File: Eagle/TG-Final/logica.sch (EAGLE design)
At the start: 1 part, among them U1 ARDUINO_SHIELDLONGPADS

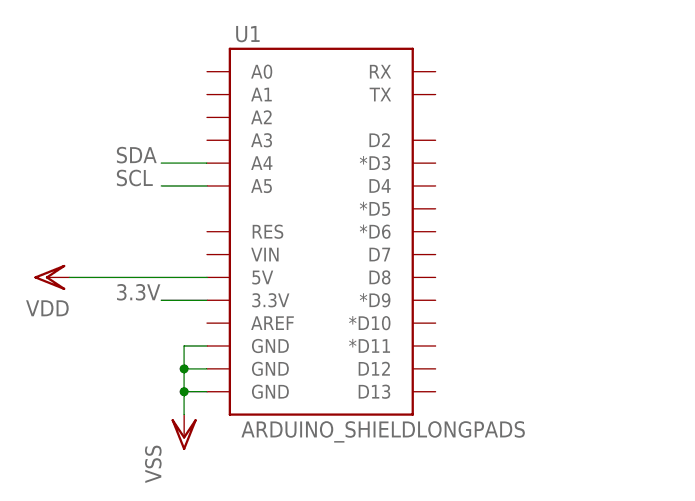
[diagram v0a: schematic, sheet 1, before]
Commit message: Esquematicos para placa logica
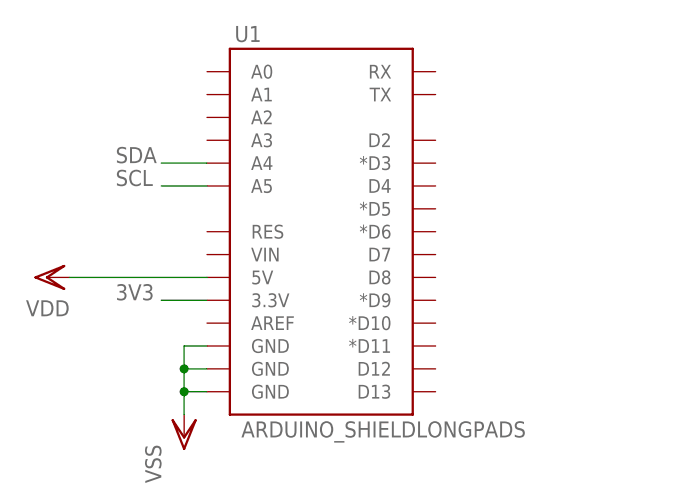
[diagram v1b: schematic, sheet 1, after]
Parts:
- added U$1: LOGIC-LEVEL-CONVERTER, aasanchez:LOGIC-LEVEL-CONVERTER
- added U$2: IMU3000COMBO, aasanchez:IMU3000COMBO
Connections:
- removed net 3.3V: U1.3.3V
- new net 3V3: U$1.LV, U$2.3V3, U1.3.3V
- new net N$1: U$1.TXI-1, U$2.SCL
- new net N$2: U$1.TXI-2, U$2.SDA
- net SCL: now also U$1.TXO-1
- net SDA: now also U$1.TXO-2
- net VDD: now also U$1.HV
- net VSS: now also U$1.GND, U$2.VSS
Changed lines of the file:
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@@
 <part name="VSS1" library="supply1" deviceset="VSS" device=""/>
 <part name="VDD1" library="supply1" deviceset="VDD" device=""/>
+<part name="U$2" library="aasanchez" deviceset="IMU3000COMBO" device=""/>
+<part name="VSS2" library="supply1" deviceset="VSS" device=""/>
+<part name="VSS3" library="supply1" deviceset="VSS" device=""/>
+<part name="VDD2" library="supply1" deviceset="VDD" device=""/>
+<part name="U$1" library="aasanchez" deviceset="LOGIC-LEVEL-CONVERTER" device=""/>
 </parts>
 <sheets>
@@
 </segment>
 </net>
-<net name="3.3V" class="0">
+<net name="3V3" class="0">
 <segment>
 <pinref part="U1" gate="G$1" pin="3.3V"/>
@@
 </plain>
 <instances>
+<instance part="U$2" gate="G$1" x="68.58" y="50.8"/>
+<instance part="VSS2" gate="G$1" x="60.96" y="45.72"/>
+<instance part="VSS3" gate="G$1" x="45.72" y="63.5" rot="R90"/>
+<instance part="VDD2" gate="G$1" x="-5.08" y="60.96" rot="R90"/>
+<instance part="U$1" gate="G$1" x="30.48" y="76.2" rot="R180"/>
 </instances>
 <busses>
 </busses>
 <nets>
+<net name="3V3" class="0">
+<segment>
+<wire x1="43.18" y1="60.96" x2="43.18" y2="53.34" width="0.1524" layer="91"/>
+<pinref part="U$2" gate="G$1" pin="3V3"/>
+<wire x1="43.18" y1="53.34" x2="63.5" y2="53.34" width="0.1524" layer="91"/>
+<pinref part="U$1" gate="G$1" pin="LV"/>
+<wire x1="43.18" y1="60.96" x2="35.56" y2="60.96" width="0.1524" layer="91"/>
+</segment>
+</net>
+<net name="VSS" class="0">
+<segment>
+<pinref part="U$2" gate="G$1" pin="VSS"/>
+<wire x1="63.5" y1="55.88" x2="60.96" y2="55.88" width="0.1524" layer="91"/>
+<wire x1="60.96" y1="55.88" x2="60.96" y2="48.26" width="0.1524" layer="91"/>
+<pinref part="VSS2" gate="G$1" pin="VSS"/>
+</segment>
+<segment>
+<pinref part="VSS3" gate="G$1" pin="VSS"/>
+<pinref part="U$1" gate="G$1" pin="GND"/>
+<wire x1="43.18" y1="63.5" x2="35.56" y2="63.5" width="0.1524" layer="91"/>
+</segment>
+</net>
+<net name="VDD" class="0">
+<segment>
+<pinref part="U$1" gate="G$1" pin="HV"/>
+<pinref part="VDD2" gate="G$1" pin="VDD"/>
+<wire x1="5.08" y1="60.96" x2="-2.54" y2="60.96" width="0.1524" layer="91"/>
+</segment>
+</net>
+<net name="SCL" class="0">
+<segment>
+<pinref part="U$1" gate="G$1" pin="TXO-1"/>
+<wire x1="5.08" y1="53.34" x2="0" y2="53.34" width="0.1524" layer="91"/>
+<label x="-5.08" y="53.34" size="1.778" layer="95"/>
+</segment>
+</net>
+<net name="SDA" class="0">
+<segment>
+<pinref part="U$1" gate="G$1" pin="TXO-2"/>
+<wire x1="5.08" y1="71.12" x2="0" y2="71.12" width="0.1524" layer="91"/>
+<label x="-5.08" y="71.12" size="1.778" layer="95"/>
+</segment>
+</net>
+<net name="N$1" class="0">
+<segment>
+<pinref part="U$1" gate="G$1" pin="TXI-1"/>
+<wire x1="35.56" y1="53.34" x2="40.64" y2="53.34" width="0.1524" layer="91"/>
+<wire x1="40.64" y1="53.34" x2="40.64" y2="50.8" width="0.1524" layer="91"/>
+<wire x1="40.64" y1="50.8" x2="58.42" y2="50.8" width="0.1524" layer="91"/>
+<wire x1="58.42" y1="50.8" x2="58.42" y2="60.96" width="0.1524" layer="91"/>
+<pinref part="U$2" gate="G$1" pin="SCL"/>
+<wire x1="58.42" y1="60.96" x2="63.5" y2="60.96" width="0.1524" layer="91"/>
+</segment>
+</net>
+<net name="N$2" class="0">
+<segment>
+<pinref part="U$1" gate="G$1" pin="TXI-2"/>
+<wire x1="35.56" y1="71.12" x2="53.34" y2="71.12" width="0.1524" layer="91"/>
+<wire x1="53.34" y1="71.12" x2="53.34" y2="58.42" width="0.1524" layer="91"/>
+<pinref part="U$2" gate="G$1" pin="SDA"/>
+<wire x1="53.34" y1="58.42" x2="63.5" y2="58.42" width="0.1524" layer="91"/>
+</segment>
+</net>
 </nets>
 </sheet>

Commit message: Fix Pins Motor 1, Avances en Esquematicos
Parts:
- added U$3: UK1122, aasanchez:UK1122
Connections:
- new net +12V: U$3.+
- new net D13: U$3.IN1, U1.D13
- new net N$13: U$3.ENA
- new net N$14: U$3.IN2
- new net N$15: U$3.IN3
- new net N$16: U$3.ENB
- new net N$17: U$3.IN4
- new net N$4: U1.D12
- new net N$5: U1.*D11
- new net N$6: U1.*D9
- new net N$8: U1.D8
- new net N$9: U1.D7
- new net SERVO-01: U1.*D10
- net 3V3: now also U$2.VCC; no longer U$2.3V3
- net VDD: now also U$3.+5
- net VSS: now also U$2.GND, U$3.-, U$3.CSA, U$3.CSB, U$3.GND; no longer U$2.VSS
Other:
- note added: "ENA"
- note added: "IN1"
- note added: "IN2"
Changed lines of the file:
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@@
 <part name="VDD2" library="supply1" deviceset="VDD" device=""/>
 <part name="U$1" library="aasanchez" deviceset="LOGIC-LEVEL-CONVERTER" device=""/>
+<part name="U$3" library="aasanchez" deviceset="UK1122" device=""/>
+<part name="VSS4" library="supply1" deviceset="VSS" device=""/>
+<part name="P+1" library="supply1" deviceset="+12V" device=""/>
+<part name="VDD3" library="supply1" deviceset="VDD" device=""/>
 </parts>
 <sheets>
@@
 <description>Arduino</description>
 <plain>
+<text x="91.44" y="45.72" size="1.778" layer="95">IN1</text>
+<text x="91.44" y="48.26" size="1.778" layer="95">IN2</text>
+<text x="91.44" y="50.8" size="1.778" layer="95">ENA</text>
 </plain>
 <instances>
@@
 <wire x1="63.5" y1="71.12" x2="58.42" y2="71.12" width="0.1524" layer="91"/>
 <label x="53.34" y="71.12" size="1.778" layer="95"/>
+</segment>
+</net>
+<net name="D13" class="0">
+<segment>
+<pinref part="U1" gate="G$1" pin="D13"/>
+<wire x1="88.9" y1="45.72" x2="91.44" y2="45.72" width="0.1524" layer="91"/>
+</segment>
+</net>
+<net name="N$4" class="0">
+<segment>
+<pinref part="U1" gate="G$1" pin="D12"/>
+<wire x1="88.9" y1="48.26" x2="91.44" y2="48.26" width="0.1524" layer="91"/>
+</segment>
+</net>
+<net name="N$5" class="0">
+<segment>
+<pinref part="U1" gate="G$1" pin="*D11"/>
+<wire x1="88.9" y1="50.8" x2="91.44" y2="50.8" width="0.1524" layer="91"/>
+</segment>
+</net>
+<net name="N$6" class="0">
+<segment>
+<pinref part="U1" gate="G$1" pin="*D9"/>
+<wire x1="88.9" y1="55.88" x2="91.44" y2="55.88" width="0.1524" layer="91"/>
+</segment>
+</net>
+<net name="SERVO-01" class="0">
+<segment>
+<pinref part="U1" gate="G$1" pin="*D10"/>
+<wire x1="88.9" y1="53.34" x2="96.52" y2="53.34" width="0.1524" layer="91"/>
+<label x="96.52" y="53.34" size="1.778" layer="95"/>
+</segment>
+</net>
+<net name="N$8" class="0">
+<segment>
+<pinref part="U1" gate="G$1" pin="D8"/>
+<wire x1="88.9" y1="58.42" x2="91.44" y2="58.42" width="0.1524" layer="91"/>
+</segment>
+</net>
+<net name="N$9" class="0">
+<segment>
+<pinref part="U1" gate="G$1" pin="D7"/>
+<wire x1="88.9" y1="60.96" x2="91.44" y2="60.96" width="0.1524" layer="91"/>
 </segment>
 </net>
@@
 <segment>
 <wire x1="43.18" y1="60.96" x2="43.18" y2="53.34" width="0.1524" layer="91"/>
-<pinref part="U$2" gate="G$1" pin="3V3"/>
+<pinref part="U$2" gate="G$1" pin="VCC"/>
 <wire x1="43.18" y1="53.34" x2="63.5" y2="53.34" width="0.1524" layer="91"/>
 <pinref part="U$1" gate="G$1" pin="LV"/>
@@
 <net name="VSS" class="0">
 <segment>
-<pinref part="U$2" gate="G$1" pin="VSS"/>
+<pinref part="U$2" gate="G$1" pin="GND"/>
 <wire x1="63.5" y1="55.88" x2="60.96" y2="55.88" width="0.1524" layer="91"/>
 <wire x1="60.96" y1="55.88" x2="60.96" y2="48.26" width="0.1524" layer="91"/>
@@
 </plain>
 <instances>
+<instance part="U$3" gate="G$1" x="0" y="0"/>
+<instance part="VSS4" gate="G$1" x="12.7" y="-10.16"/>
+<instance part="P+1" gate="1" x="0" y="-2.54" rot="R90"/>
+<instance part="VDD3" gate="G$1" x="20.32" y="-17.78" rot="R180"/>
 </instances>
 <busses>
 </busses>
 <nets>
+<net name="VSS" class="0">
+<segment>
+<pinref part="U$3" gate="G$1" pin="-"/>
+<wire x1="7.62" y1="0" x2="7.62" y2="-2.54" width="0.1524" layer="91"/>
+<wire x1="7.62" y1="-2.54" x2="12.7" y2="-2.54" width="0.1524" layer="91"/>
+<pinref part="U$3" gate="G$1" pin="GND"/>
+<wire x1="12.7" y1="-2.54" x2="17.78" y2="-2.54" width="0.1524" layer="91"/>
+<wire x1="17.78" y1="-2.54" x2="17.78" y2="0" width="0.1524" layer="91"/>
+<wire x1="17.78" y1="-2.54" x2="30.48" y2="-2.54" width="0.1524" layer="91"/>
+<pinref part="U$3" gate="G$1" pin="CSA"/>
+<wire x1="30.48" y1="-2.54" x2="30.48" y2="0" width="0.1524" layer="91"/>
+<pinref part="U$3" gate="G$1" pin="CSB"/>
+<wire x1="40.64" y1="0" x2="40.64" y2="-2.54" width="0.1524" layer="91"/>
+<wire x1="40.64" y1="-2.54" x2="30.48" y2="-2.54" width="0.1524" layer="91"/>
+<pinref part="VSS4" gate="G$1" pin="VSS"/>
+<wire x1="12.7" y1="-7.62" x2="12.7" y2="-2.54" width="0.1524" layer="91"/>
+<junction x="12.7" y="-2.54"/>
+<junction x="17.78" y="-2.54"/>
+<junction x="30.48" y="-2.54"/>
+</segment>
+</net>
+<net name="+12V" class="0">
+<segment>
+<pinref part="P+1" gate="1" pin="+12V"/>
+<wire x1="2.54" y1="-2.54" x2="5.08" y2="-2.54" width="0.1524" layer="91"/>
+<pinref part="U$3" gate="G$1" pin="+"/>
+<wire x1="5.08" y1="-2.54" x2="5.08" y2="0" width="0.1524" layer="91"/>
+</segment>
+</net>
+<net name="VDD" class="0">
+<segment>
+<pinref part="VDD3" gate="G$1" pin="VDD"/>
+<pinref part="U$3" gate="G$1" pin="+5"/>
+<wire x1="20.32" y1="-15.24" x2="20.32" y2="0" width="0.1524" layer="91"/>
+</segment>
+</net>
+<net name="D13" class="0">
+<segment>
+<pinref part="U$3" gate="G$1" pin="IN1"/>
+<wire x1="22.86" y1="0" x2="22.86" y2="-7.62" width="0.1524" layer="91"/>
+<label x="22.86" y="-7.62" size="1.778" layer="95" rot="R270"/>
+</segment>
+</net>
+<net name="N$13" class="0">
+<segment>
+<pinref part="U$3" gate="G$1" pin="ENA"/>
+<wire x1="25.4" y1="0" x2="25.4" y2="-7.62" width="0.1524" layer="91"/>
+</segment>
+</net>
+<net name="N$14" class="0">
+<segment>
+<pinref part="U$3" gate="G$1" pin="IN2"/>
+<wire x1="27.94" y1="0" x2="27.94" y2="-7.62" width="0.1524" layer="91"/>
+</segment>
+</net>
+<net name="N$15" class="0">
+<segment>
+<pinref part="U$3" gate="G$1" pin="IN3"/>
+<wire x1="33.02" y1="0" x2="33.02" y2="-7.62" width="0.1524" layer="91"/>
+</segment>
+</net>
+<net name="N$16" class="0">
+<segment>
+<pinref part="U$3" gate="G$1" pin="ENB"/>
+<wire x1="35.56" y1="0" x2="35.56" y2="-7.62" width="0.1524" layer="91"/>
+</segment>
+</net>
+<net name="N$17" class="0">
+<segment>
+<pinref part="U$3" gate="G$1" pin="IN4"/>
+<wire x1="38.1" y1="0" x2="38.1" y2="-7.62" width="0.1524" layer="91"/>
+</segment>
+</net>
 </nets>
 </sheet>

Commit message: Placa de Actuadores y Otros
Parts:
- added U$4: BASE, aasanchez:BASE
- renumbered U$3 to L298
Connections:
- removed net N$13: L298.ENA
- removed net N$14: L298.IN2
- removed net N$15: L298.IN3
- removed net N$16: L298.ENB
- removed net N$17: L298.IN4
- removed net N$4: U1.D12
- removed net N$5: U1.*D11
- removed net N$6: U1.*D9
- removed net N$8: U1.D8
- removed net N$9: U1.D7
- new net D11: L298.ENA, U1.*D11
- new net D12: L298.IN2, U1.D12
- new net D7: L298.IN4, U1.D7
- new net D8: L298.IN3, U1.D8
- new net D9: L298.ENB, U1.*D9
- new net SERVO-02: U1.*D6
- new net SERVO-03: U1.*D5
- new net SERVO-04: U1.*D3
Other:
- note added: "ENB"
- note added: "IN3"
- note added: "IN4"
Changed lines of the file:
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@@
 <part name="VDD2" library="supply1" deviceset="VDD" device=""/>
 <part name="U$1" library="aasanchez" deviceset="LOGIC-LEVEL-CONVERTER" device=""/>
-<part name="U$3" library="aasanchez" deviceset="UK1122" device=""/>
+<part name="L298" library="aasanchez" deviceset="UK1122" device=""/>
 <part name="VSS4" library="supply1" deviceset="VSS" device=""/>
 <part name="P+1" library="supply1" deviceset="+12V" device=""/>
 <part name="VDD3" library="supply1" deviceset="VDD" device=""/>
+<part name="U$4" library="aasanchez" deviceset="BASE" device=""/>
 </parts>
 <sheets>
@@
 <text x="91.44" y="48.26" size="1.778" layer="95">IN2</text>
 <text x="91.44" y="50.8" size="1.778" layer="95">ENA</text>
+<text x="91.44" y="55.88" size="1.778" layer="95">ENB</text>
+<text x="91.44" y="58.42" size="1.778" layer="95">IN3</text>
+<text x="91.44" y="60.96" size="1.778" layer="95">IN4</text>
 </plain>
 <instances>
@@
 <instance part="VSS1" gate="G$1" x="60.96" y="40.64"/>
 <instance part="VDD1" gate="G$1" x="45.72" y="58.42" rot="R90"/>
+<instance part="U$4" gate="G$1" x="106.68" y="40.64"/>
 </instances>
 <busses>
@@
 </segment>
 </net>
-<net name="N$4" class="0">
+<net name="D12" class="0">
 <segment>
 <pinref part="U1" gate="G$1" pin="D12"/>
@@
 </segment>
 </net>
-<net name="N$5" class="0">
+<net name="D11" class="0">
 <segment>
 <pinref part="U1" gate="G$1" pin="*D11"/>
@@
 </segment>
 </net>
-<net name="N$6" class="0">
+<net name="D9" class="0">
 <segment>
 <pinref part="U1" gate="G$1" pin="*D9"/>
@@
 </segment>
 </net>
-<net name="N$8" class="0">
+<net name="D8" class="0">
 <segment>
 <pinref part="U1" gate="G$1" pin="D8"/>
@@
 </segment>
 </net>
-<net name="N$9" class="0">
+<net name="D7" class="0">
 <segment>
 <pinref part="U1" gate="G$1" pin="D7"/>
 <wire x1="88.9" y1="60.96" x2="91.44" y2="60.96" width="0.1524" layer="91"/>
+</segment>
+</net>
+<net name="SERVO-02" class="0">
+<segment>
+<pinref part="U1" gate="G$1" pin="*D6"/>
+<wire x1="88.9" y1="63.5" x2="96.52" y2="63.5" width="0.1524" layer="91"/>
+<label x="96.52" y="63.5" size="1.778" layer="95"/>
+</segment>
+</net>
+<net name="SERVO-03" class="0">
+<segment>
+<pinref part="U1" gate="G$1" pin="*D5"/>
+<wire x1="88.9" y1="66.04" x2="96.52" y2="66.04" width="0.1524" layer="91"/>
+<label x="96.52" y="66.04" size="1.778" layer="95"/>
+</segment>
+</net>
+<net name="SERVO-04" class="0">
+<segment>
+<pinref part="U1" gate="G$1" pin="*D3"/>
+<wire x1="88.9" y1="71.12" x2="96.52" y2="71.12" width="0.1524" layer="91"/>
+<label x="96.52" y="71.12" size="1.778" layer="95"/>
 </segment>
 </net>
@@
 </plain>
 <instances>
-<instance part="U$3" gate="G$1" x="0" y="0"/>
-<instance part="VSS4" gate="G$1" x="12.7" y="-10.16"/>
+<instance part="L298" gate="G$1" x="0" y="0"/>
+<instance part="VSS4" gate="G$1" x="12.7" y="-17.78"/>
 <instance part="P+1" gate="1" x="0" y="-2.54" rot="R90"/>
 <instance part="VDD3" gate="G$1" x="20.32" y="-17.78" rot="R180"/>
@@
 <net name="VSS" class="0">
 <segment>
-<pinref part="U$3" gate="G$1" pin="-"/>
+<pinref part="L298" gate="G$1" pin="-"/>
 <wire x1="7.62" y1="0" x2="7.62" y2="-2.54" width="0.1524" layer="91"/>
 <wire x1="7.62" y1="-2.54" x2="12.7" y2="-2.54" width="0.1524" layer="91"/>
-<pinref part="U$3" gate="G$1" pin="GND"/>
+<pinref part="L298" gate="G$1" pin="GND"/>
 <wire x1="12.7" y1="-2.54" x2="17.78" y2="-2.54" width="0.1524" layer="91"/>
 <wire x1="17.78" y1="-2.54" x2="17.78" y2="0" width="0.1524" layer="91"/>
 <wire x1="17.78" y1="-2.54" x2="30.48" y2="-2.54" width="0.1524" layer="91"/>
-<pinref part="U$3" gate="G$1" pin="CSA"/>
+<pinref part="L298" gate="G$1" pin="CSA"/>
 <wire x1="30.48" y1="-2.54" x2="30.48" y2="0" width="0.1524" layer="91"/>
-<pinref part="U$3" gate="G$1" pin="CSB"/>
+<pinref part="L298" gate="G$1" pin="CSB"/>
 <wire x1="40.64" y1="0" x2="40.64" y2="-2.54" width="0.1524" layer="91"/>
 <wire x1="40.64" y1="-2.54" x2="30.48" y2="-2.54" width="0.1524" layer="91"/>
 <pinref part="VSS4" gate="G$1" pin="VSS"/>
-<wire x1="12.7" y1="-7.62" x2="12.7" y2="-2.54" width="0.1524" layer="91"/>
+<wire x1="12.7" y1="-15.24" x2="12.7" y2="-2.54" width="0.1524" layer="91"/>
 <junction x="12.7" y="-2.54"/>
 <junction x="17.78" y="-2.54"/>
@@
 <pinref part="P+1" gate="1" pin="+12V"/>
 <wire x1="2.54" y1="-2.54" x2="5.08" y2="-2.54" width="0.1524" layer="91"/>
-<pinref part="U$3" gate="G$1" pin="+"/>
+<pinref part="L298" gate="G$1" pin="+"/>
 <wire x1="5.08" y1="-2.54" x2="5.08" y2="0" width="0.1524" layer="91"/>
 </segment>
@@
 <segment>
 <pinref part="VDD3" gate="G$1" pin="VDD"/>
-<pinref part="U$3" gate="G$1" pin="+5"/>
+<pinref part="L298" gate="G$1" pin="+5"/>
 <wire x1="20.32" y1="-15.24" x2="20.32" y2="0" width="0.1524" layer="91"/>
 </segment>
@@
 <net name="D13" class="0">
 <segment>
-<pinref part="U$3" gate="G$1" pin="IN1"/>
+<pinref part="L298" gate="G$1" pin="IN1"/>
 <wire x1="22.86" y1="0" x2="22.86" y2="-7.62" width="0.1524" layer="91"/>
 <label x="22.86" y="-7.62" size="1.778" layer="95" rot="R270"/>
 </segment>
 </net>
-<net name="N$13" class="0">
-<segment>
-<pinref part="U$3" gate="G$1" pin="ENA"/>
+<net name="D11" class="0">
+<segment>
+<pinref part="L298" gate="G$1" pin="ENA"/>
 <wire x1="25.4" y1="0" x2="25.4" y2="-7.62" width="0.1524" layer="91"/>
-</segment>
-</net>
-<net name="N$14" class="0">
-<segment>
-<pinref part="U$3" gate="G$1" pin="IN2"/>
+<label x="25.4" y="-7.62" size="1.778" layer="95" rot="R270"/>
+</segment>
+</net>
+<net name="D12" class="0">
+<segment>
+<pinref part="L298" gate="G$1" pin="IN2"/>
 <wire x1="27.94" y1="0" x2="27.94" y2="-7.62" width="0.1524" layer="91"/>
-</segment>
-</net>
-<net name="N$15" class="0">
-<segment>
-<pinref part="U$3" gate="G$1" pin="IN3"/>
+<label x="27.94" y="-7.62" size="1.778" layer="95" rot="R270"/>
+</segment>
+</net>
+<net name="D8" class="0">
+<segment>
+<pinref part="L298" gate="G$1" pin="IN3"/>
 <wire x1="33.02" y1="0" x2="33.02" y2="-7.62" width="0.1524" layer="91"/>
-</segment>
-</net>
-<net name="N$16" class="0">
-<segment>
-<pinref part="U$3" gate="G$1" pin="ENB"/>
+<label x="33.02" y="-7.62" size="1.778" layer="95" rot="R270"/>
+</segment>
+</net>
+<net name="D9" class="0">
+<segment>
+<pinref part="L298" gate="G$1" pin="ENB"/>
 <wire x1="35.56" y1="0" x2="35.56" y2="-7.62" width="0.1524" layer="91"/>
-</segment>
-</net>
-<net name="N$17" class="0">
-<segment>
-<pinref part="U$3" gate="G$1" pin="IN4"/>
+<label x="35.56" y="-7.62" size="1.778" layer="95" rot="R270"/>
+</segment>
+</net>
+<net name="D7" class="0">
+<segment>
+<pinref part="L298" gate="G$1" pin="IN4"/>
 <wire x1="38.1" y1="0" x2="38.1" y2="-7.62" width="0.1524" layer="91"/>
-</segment>
-</net>
+<label x="38.1" y="-7.62" size="1.778" layer="95" rot="R270"/>
+</segment>
+</net>
